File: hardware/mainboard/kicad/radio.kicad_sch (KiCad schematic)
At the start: 4 parts, among them J11 J_GPS, U10 E22-400T22S

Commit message: Kartonaut: Name, Missionsabzeichen, Bestückungsdruck neu, Lötstopp blau
- Projekt heißt Kartonaut (Karton + Astronaut); Flüge werden hochgezählt, Erstflug = Kartonaut 1
- Abzeichen als Polygone in hardware/mainboard/kicad/logo.py, SVGs in docs/brand/
- spacecode/ -> firmware/, Bodenstation-Repo groundcode -> kartonaut-ground (Links, .gitignore)
- gen_pcb.py silk: Bestückungsdruck nur neu setzen, auf der gerouteten Platine; 1,0 mm Schrift,
  freie Plätze statt Überlappungen, Kurznamen an den Steckern, Testpunkte mit Netznamen,
  kleines Abzeichen vorn; hinten Abzeichen 20 mm und Steckerbelegung
- Stackup JLC04161H-7628 mit blauem Lötstopp im Board, Renders mit Stackup-Farben
- DRC-Druckwarnungen 167 -> 14 (Rest aus Footprint-Umrissen)

Co-Authored-By: Claude Opus 5.5 <noreply@anthropic.com>
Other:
- company: Mission Space -> Kartonaut
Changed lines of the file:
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@@
 		(date "2026-10-21")
 		(rev "B")
-		(company "Mission Space")
+		(company "Kartonaut")
 		(comment 1 "LoRa E22-400T22S an Serial8, GPS an Serial1")
 		(comment 2 "erzeugt aus circuit.py (gen_schematic.py)")

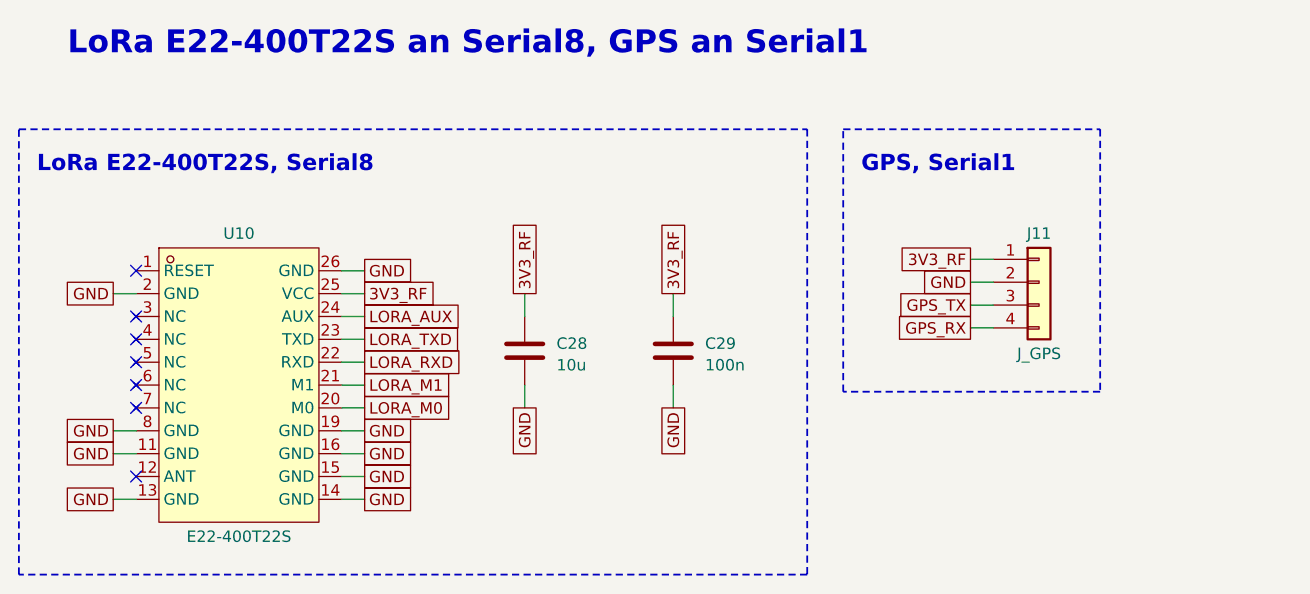
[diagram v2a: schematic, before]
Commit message: Mainboard rev B1: Review A1-A8 und Entscheidungen E1-E10 eingearbeitet, 2S-Pfad als F.Cu-Flaechen, 28 Verbindungen offen
Schaltung (circuit.py, ERC 0, Netzliste gegen README §4 OK): Hold-up hinter D1, EN-Teiler 330k/115k,
P-FET-Lastschalter je Akku, Polyfuse je Akku, Kelvin-Shunt mit INA239 an SPI1, BMP390 an SPI1,
74HC138/74HC4051 mit gemeinsamer Adresse, J_STACK 2x10 mit LDO 3V3_EXP, 1S-Lader MCP73831,
J_CHG2, vier Pyro-Kanaele (3/4 DNP), vierter Servo, alle Servos und Rollmotor an VSERVO,
3V3_SENS, eine WS2812B-Kette, Summer Pin 37, E22 NRST Pin 6; 166 Bauteile.

Platine (gen_pcb.py): neue Platzierung, 2S-Pfad, Pyro-Ausgaenge und VSYS_IN als F.Cu-Flaechen mit
Sperrflaechen fuer Freerouting, Strom-Klasse nur F.Cu, IMU-Zone 5 mm, patch mit Umweg ueber In2.
DRC 0 Fehler, Paritaet 0, kein 2S-Netz auf In2; 28 offene Verbindungen, Liste in kicad/README.md §5.5.
Spezifikation README.md und kicad/README.md auf B1 nachgezogen, review_check_layout.py fuer B1.

Co-Authored-By: Claude Opus 5.5 <noreply@anthropic.com>
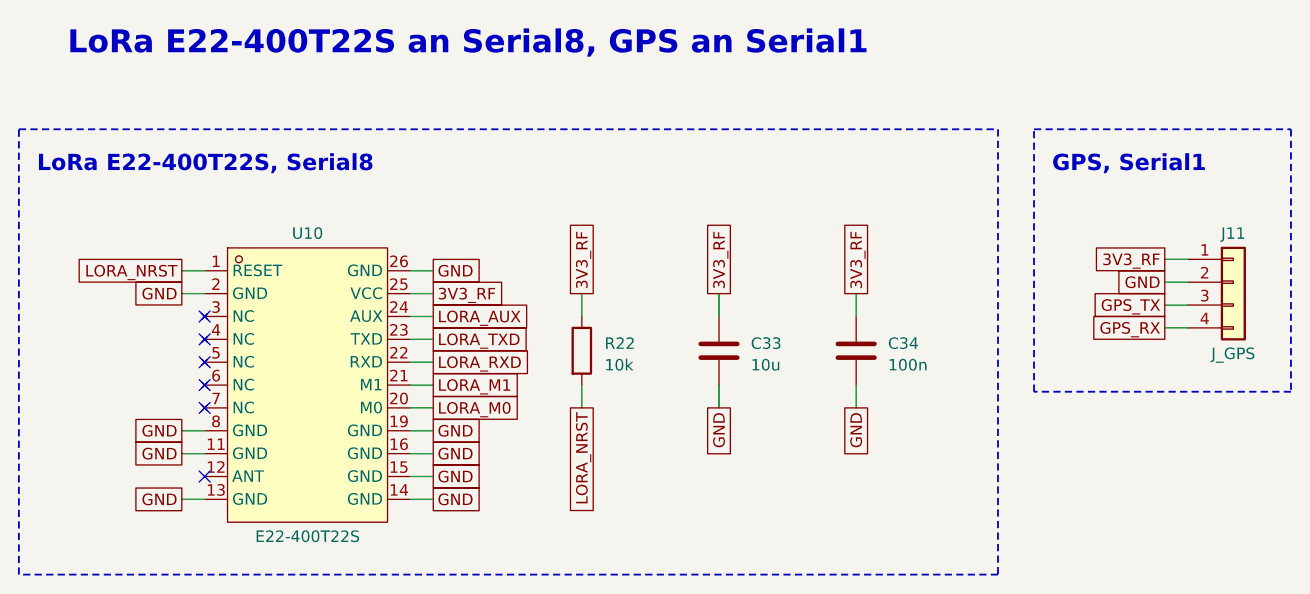
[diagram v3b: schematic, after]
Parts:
- removed C28: 10u, Capacitor_SMD:C_0805_2012Metric, symbol Device:C
- removed C29: 100n, Capacitor_SMD:C_0603_1608Metric, symbol Device:C
- added C33: 10u, Capacitor_SMD:C_0805_2012Metric, symbol Device:C
- added C34: 100n, Capacitor_SMD:C_0603_1608Metric, symbol Device:C
- added R22: 10k, Resistor_SMD:R_0603_1608Metric, symbol Device:R
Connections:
- net 3V3_RF: now also C33.1, C34.1, R22.1
- net GND: now also C33.2, C34.2
- net LORA_NRST: now reaches U10.1 (RESET)
- net LORA_NRST: now also R22.2
- no-connect marks 7 -> 6
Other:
- moved on the sheet: J11, U10
